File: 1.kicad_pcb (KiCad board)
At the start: 2 copper layers, 77.5 x 40.6 mm, 32 parts, among them IC1 LTC4361IDC-2#TRMPBF, IC2 SI1470DH-T1-E3, IC3 SI1470DH-T1-E3, IC4 LTC4361IDC-2#TRMPBF, J1 Screw_Terminal_01x03, J2 Screw_Terminal_01x01, J3 Screw_Terminal_01x01, J4 ON2, J5 ON1, U1 LTC2990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

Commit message: Patch
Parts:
- removed IC1, IC4: LTC4361IDC-2#TRMPBF, Library:SON45P200X200X80-9N-D
- removed IC2, IC3: SI1470DH-T1-E3, Library:SOT65P210X110-6N
- removed J4: ON2, Connector_PinHeader_1.00mm:PinHeader_1x01_P1.00mm_Vertical
- removed J5: ON1, Connector_PinHeader_1.00mm:PinHeader_1x01_P1.00mm_Vertical
- removed R3, R4: 0.025, 0.025 ohm rst:CRA2512-FZ-R025ELF
- R5, R6, R7: value 60m -> 50m; footprint 60 mil rst:RESC7146X175N -> 50m RST:RESC3216X88N
- moved U2 20.7 mm to (172.5, 78.7)
- moved SCLSDA1 20.6 mm to (175.0, 69.7)
- moved R6 20.6 mm to (171.7, 84.3)
- moved SCLSDA2 20.4 mm to (179.1, 89.0)
- moved R7 20.4 mm to (172.7, 100.3)
- moved U3 20.2 mm to (172.9, 94.0)
- moved U1 5.14 mm to (140.6, 73.7)
- moved R5 3.04 mm to (140.0, 79.1)
- moved C1 2.54 mm to (139.7, 96.5), turned to -90 degrees
- moved SCLSDA3 2.21 mm to (147.3, 70.8)
- moved J2 1.27 mm to (134.6, 71.1)
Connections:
- R6 pad 1: Net-(IC1-Pad3) -> Net-(Buck_IC1-Pad4)
- R7 pad 1: Net-(IC3-Pad4) -> Net-(Boost_IC1-Pad5)
- U2 pad 1: Net-(IC1-Pad3) -> Net-(Buck_IC1-Pad4)
- U2 pad 10: Net-(IC1-Pad3) -> Net-(Buck_IC1-Pad4)
- U3 pad 1: Net-(IC3-Pad4) -> Net-(Boost_IC1-Pad5)
- U3 pad 10: Net-(IC3-Pad4) -> Net-(Boost_IC1-Pad5)
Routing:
- net Earth: track 140.9 -> 90.6 mm, vias 7 -> 5
- net Net-(IC3-Pad4): track 38.0 -> 0.00 mm
- net Net-(IC1-Pad3): track 35.2 -> 0.00 mm
- net Net-(J1-Pad2): track 22.7 -> 0.00 mm
- net Net-(Buck_IC1-Pad4): track 60.0 -> 38.8 mm
- net Net-(Boost_IC1-Pad5): track 61.7 -> 43.2 mm
- net Net-(IC3-Pad1): track 16.5 -> 0.00 mm
- net Net-(Boost_IC1-Pad1): track 67.0 -> 52.2 mm
- net Net-(IC1-Pad7): track 14.1 -> 0.00 mm
- net Net-(J1-Pad1): track 16.3 -> 3.87 mm
- net Net-(SCLSDA2-Pad1): track 6.76 -> 19.0 mm
- net Net-(SCLSDA2-Pad2): track 7.41 -> 0.00 mm
- net Net-(J2-Pad1): track 27.3 -> 20.1 mm
- net Net-(IC3-Pad3): track 6.06 -> 0.00 mm
- net Net-(SCLSDA3-Pad1): track 5.83 -> 0.00 mm
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- removed copper zone on B.Cu, net Earth

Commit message: v1
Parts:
- Boost_IC1: footprint Boost LTC3426:SOT95P280X90-6N -> libs:SOT95P280X90-6N
- Buck_IC1: footprint BUck TPS62203DBVT:SOT95P280X145-5N -> libs:SOT95P280X145-5N
- C1, C4: footprint capa 10uf:CAPAE530X610N -> libs:CAPAE530X610N
- C2: footprint cap 22uF low esr and esl:C3216_Commercial -> libs:C3216_Commercial
- C3: footprint cap 4.7uf:C1210 -> libs:C1210
- D1: footprint Schottky dd:DIOM5026X220N -> libs:DIOM5026X220N
- J1: footprint TerminalBlock_MetzConnect:TerminalBlock_MetzConnect_Type055_RT01503HDWU_1x03_P5.00mm_Horizontal -> libs:TerminalBlock_MetzConnect_Type055_RT01503HDWU_1x03_P5.00mm_Horizontal
- J2, J3: footprint Connector_Pin:Pin_D1.3mm_L11.0mm_LooseFit -> libs:Pin_D1.3mm_L11.0mm_LooseFit
- L1: footprint indc 2.2uH:IHLP2020CZER2R2M8A -> libs:IHLP2020CZER2R2M8A
- L2: footprint indc 10uH crct:SRN1060-100M -> libs:SRN1060-100M
- R1: footprint rst 95.3k:RESC2012X60N -> libs:RESC2012X60N
- R2: footprint rst 30.9k:RC0603FR-0730K9L -> libs:RC0603FR-0730K9L
- R5, R6, R7: footprint 50m RST:RESC3216X88N -> libs:RESC3216X88N
- SCLSDA1, SCLSDA2, SCLSDA3, SHDN1: footprint Connector_PinHeader_1.00mm:PinHeader_1x02_P1.00mm_Vertical -> libs:PinHeader_1x02_P1.00mm_Vertical
- U1, U2, U3: footprint MON & PROTECC:SOP50P490X110-10N -> libs:SOP50P490X110-10N
- moved J1 21.7 mm to (182.9, 81.4)
- moved SCLSDA2 4.83 mm to (174.3, 88.6), turned to -90 degrees
- moved SHDN1 4.76 mm to (137.2, 89.5)
- moved SCLSDA1 2.88 mm to (174.0, 72.4), turned to -90 degrees
- moved R7 0.47 mm to (172.2, 100.3)
- moved R5 0.07 mm to (139.9, 79.1)
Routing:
- net Net-(J1-Pad2): track 0.00 -> 24.8 mm
- net Earth: track 90.6 -> 112.1 mm
- net Net-(Buck_IC1-Pad4): track 38.8 -> 60.0 mm
- net Net-(Boost_IC1-Pad5): track 43.2 -> 62.3 mm
- net Net-(SCLSDA2-Pad1): track 19.0 -> 3.31 mm
- net Net-(J1-Pad1): track 3.87 -> 14.9 mm
- net Net-(Boost_IC1-Pad1): track 52.2 -> 43.4 mm
- net Net-(SCLSDA3-Pad1): track 0.00 -> 5.98 mm
- net Net-(Boost_IC1-Pad4): track 25.7 -> 21.9 mm
- net Net-(J2-Pad1): track 20.1 -> 16.4 mm
- net Net-(SCLSDA1-Pad2): track 7.82 -> 4.14 mm
- net Net-(SCLSDA2-Pad2): track 0.00 -> 3.26 mm
- net Net-(Buck_IC1-Pad3): track 15.8 -> 13.3 mm
- net Net-(SCLSDA1-Pad1): track 6.32 -> 4.35 mm
- net Net-(SCLSDA3-Pad2): track 5.54 -> 7.49 mm
- added copper zone on B.Cu, net Earth
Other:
- board size 77.5 x 40.6 mm -> 55.9 x 35.6 mm

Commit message: Fixes + Patches
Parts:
- moved C1 0.32 mm to (140.0, 96.4)
- renumbered SCLSDA1 to I2C1, SCLSDA2 to I2C2, SCLSDA3 to I2C3, SHDN1 to SDN
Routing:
- net Earth: track 112.1 -> 70.7 mm
- net Net-(Boost_IC1-Pad1): track 43.4 -> 47.1 mm
- net Net-(J2-Pad1): track 16.4 -> 20.0 mm
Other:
- board text added: "CubeSat EPS Regulation Module"
- board text added: "GEC Barton Hill"

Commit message: Fix
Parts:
- removed SDN: EN, libs:PinHeader_1x02_P1.00mm_Vertical
- added R3: 1M, 1MEGA RST:RESC1608X55N, F.Cu at (147.0, 86.7)
- Boost_IC1: footprint libs:SOT95P280X90-6N -> Boost LTC3426:SOT95P280X90-6N
- Buck_IC1: footprint libs:SOT95P280X145-5N -> BUck TPS62203DBVT:SOT95P280X145-5N
- C1, C4: footprint libs:CAPAE530X610N -> capa 10uf:CAPAE530X610N
- C2: footprint libs:C3216_Commercial -> cap 22uF low esr and esl:C3216_Commercial
- C3: footprint libs:C1210 -> cap 4.7uf:C1210
- D1: footprint libs:DIOM5026X220N -> Schottky dd:DIOM5026X220N
- I2C1, I2C2, I2C3: footprint libs:PinHeader_1x02_P1.00mm_Vertical -> Connector_PinHeader_1.00mm:PinHeader_1x02_P1.00mm_Vertical
- J1: footprint libs:TerminalBlock_MetzConnect_Type055_RT01503HDWU_1x03_P5.00mm_Horizontal -> TerminalBlock_MetzConnect:TerminalBlock_MetzConnect_Type055_RT01503HDWU_1x03_P5.00mm_Horizontal
- J2, J3: footprint libs:Pin_D1.3mm_L11.0mm_LooseFit -> Connector_Pin:Pin_D1.3mm_L11.0mm_LooseFit
- L1: footprint libs:IHLP2020CZER2R2M8A -> indc 2.2uH:IHLP2020CZER2R2M8A
- L2: footprint libs:SRN1060-100M -> indc 10uH crct:SRN1060-100M
- R1: footprint libs:RESC2012X60N -> rst 95.3k:RESC2012X60N
- R2: footprint libs:RC0603FR-0730K9L -> rst 30.9k:RC0603FR-0730K9L
- R5, R6, R7: footprint libs:RESC3216X88N -> 50m RST:RESC3216X88N
- U1, U2, U3: footprint libs:SOP50P490X110-10N -> MON & PROTECC:SOP50P490X110-10N
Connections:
- Buck_IC1 pad 3: Net-(Buck_IC1-Pad3) -> Net-(Boost_IC1-Pad1)
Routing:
- net Net-(Buck_IC1-Pad3): track 13.3 -> 0.00 mm
- net Net-(Boost_IC1-Pad4): track 21.9 -> 14.9 mm
- net Net-(Boost_IC1-Pad1): track 47.1 -> 53.8 mm
- net Net-(Boost_IC1-Pad6): track 12.9 -> 15.8 mm
- net Earth: track 70.7 -> 68.3 mm, vias 5 -> 6

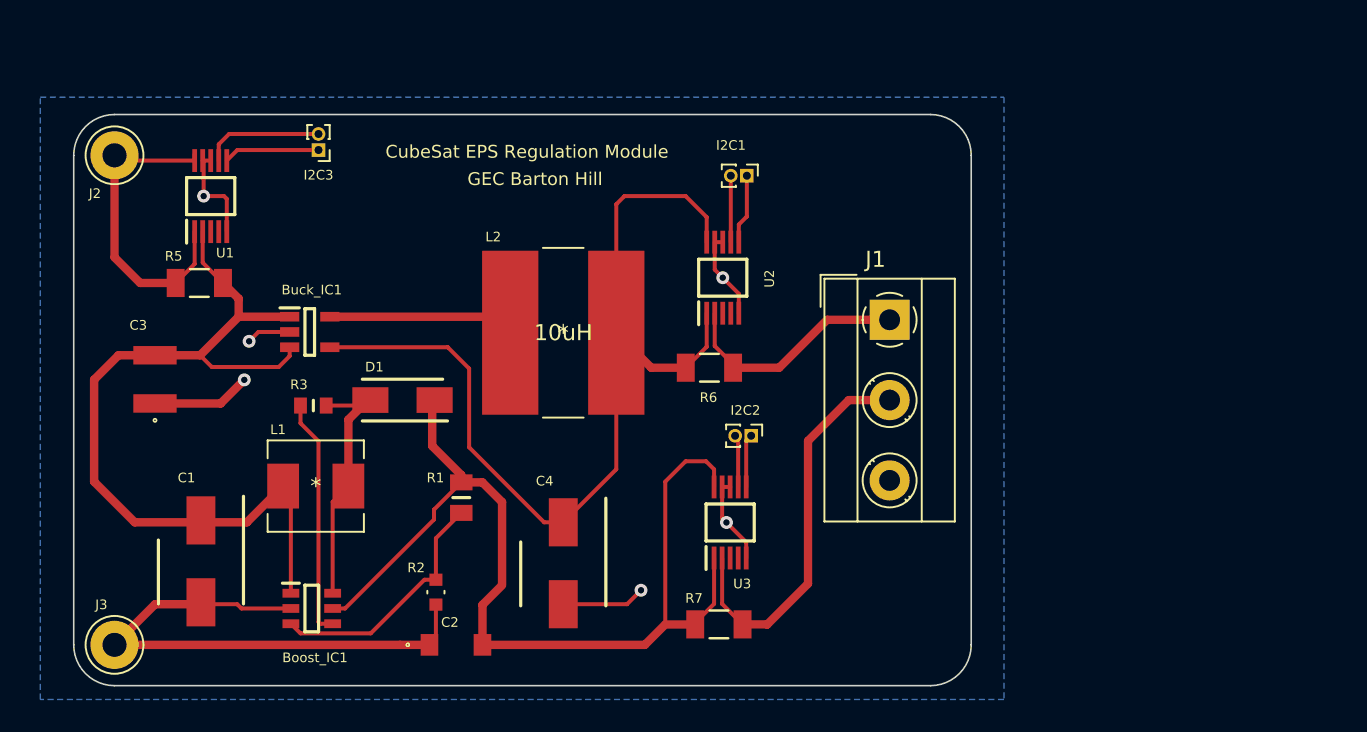
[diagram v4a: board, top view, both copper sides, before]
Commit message: Replaced Al elec caps
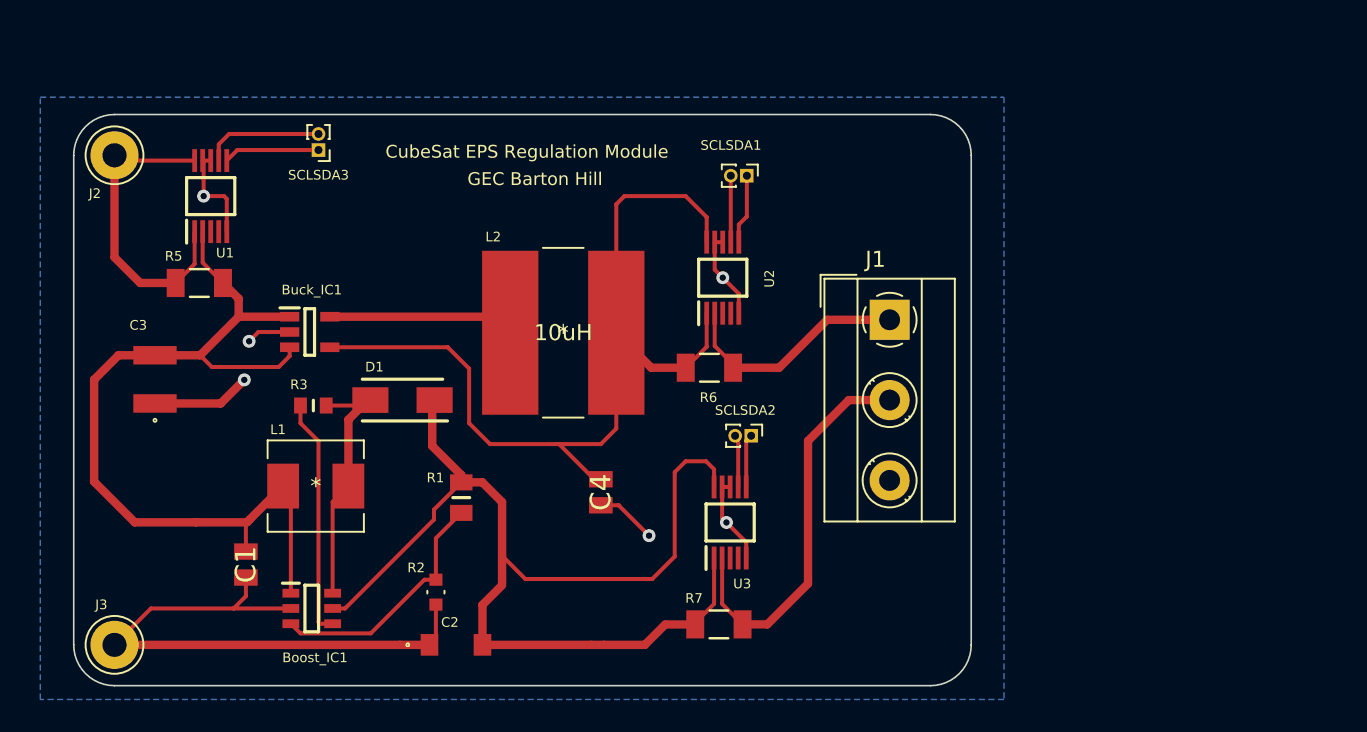
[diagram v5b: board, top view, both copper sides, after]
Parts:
- C1, C4: footprint capa 10uf:CAPAE530X610N -> 10uF MLCC:CAPC2012X94N
- moved C4 5.00 mm to (164.9, 92.1)
- moved C1 2.81 mm to (142.8, 96.6)
- renumbered I2C1 to SCLSDA1, I2C2 to SCLSDA2, I2C3 to SCLSDA3
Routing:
- net Net-(Boost_IC1-Pad5): track 62.3 -> 70.0 mm
- net Net-(Buck_IC1-Pad4): track 60.2 -> 57.3 mm
- net Net-(Boost_IC1-Pad1): track 53.8 -> 55.7 mm
- net Earth: track 68.3 -> 68.9 mm

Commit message: Fixed routing issues and naming of pins
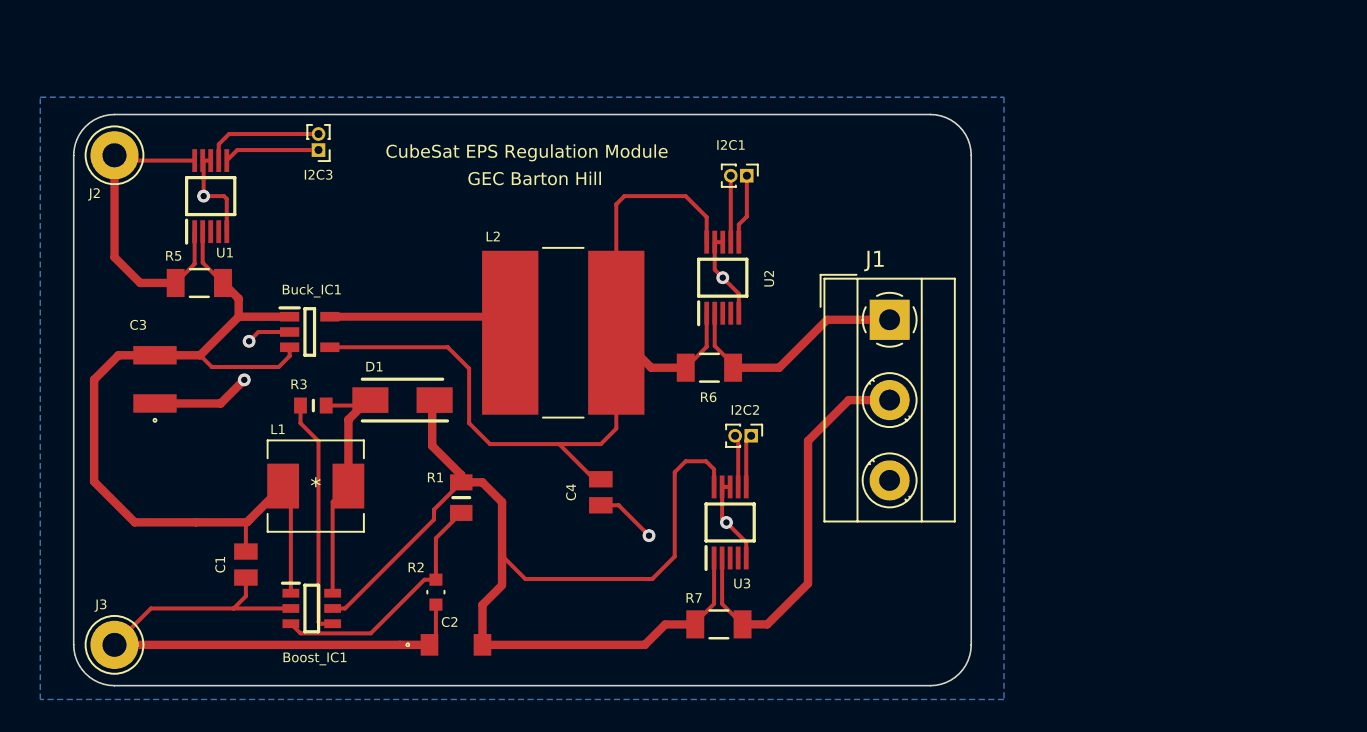
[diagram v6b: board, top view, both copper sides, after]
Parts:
- renumbered SCLSDA1 to I2C1, SCLSDA2 to I2C2, SCLSDA3 to I2C3
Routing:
- net Earth: track 68.9 -> 66.5 mm

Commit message: FInal...I guess
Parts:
- D1: footprint Schottky dd:DIOM5026X220N -> Schottky DD with stock:DIOM5126X265N
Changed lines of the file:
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@@
       (sketchpadsonfab false)
       (subtractmaskfromsilk false)
-      (outputformat 4)
+      (outputformat 1)
       (mirror false)
       (drillshape 0)
       (scaleselection 1)
-      (outputdirectory "/home/arch1/Desktop/")
+      (outputdirectory "/mnt/DAA829C1A8299CCF/EEE/S7/PROJ/voltage-regulator-module/Gerbers/")
     )
   )
@@
     )
   )
-  (footprint "Schottky dd:DIOM5026X220N" (layer "F.Cu")
+  (footprint "Schottky DD with stock:DIOM5126X265N" (layer "F.Cu")
     (at 152.55 86.36 180)
-    (descr "PMDS_SOD106")
-    (tags "Schottky Diode")
-    (property "Sheetfile" "1.kicad_sch")
-    (property "Sheetname" "")
-    (attr smd)
-    (fp_text reference "D1" (at 1.75 2.06 180) (layer "F.SilkS")
-      (effects (font (size 0.6 0.6) (thickness 0.15)))
+    (descr "SMA")
+    (tags "Diode")
+    (property "Sheetfile" "1.kicad_sch")
+    (property "Sheetname" "")
+    (attr smd)
+    (fp_text reference "D1" (at 0 0 180) (layer "F.SilkS")
+      (effects (font (size 1.27 1.27) (thickness 0.254)))
     )
     (fp_text value "D_Schottky" (at 0 0 180) (layer "F.SilkS") hide
@@
       (effects (font (size 1.27 1.27) (thickness 0.254)))
     )
-    (fp_line (start 2.5 -1.3) (end -2.8 -1.3) (layer "F.SilkS") (width 0.2))
-    (fp_line (start -2.5 1.3) (end 2.5 1.3) (layer "F.SilkS") (width 0.2))
-    (fp_line (start -3.375 1.65) (end -3.375 -1.65) (layer "F.CrtYd") (width 0.05))
-    (fp_line (start -3.375 -1.65) (end 3.375 -1.65) (layer "F.CrtYd") (width 0.05))
-    (fp_line (start 3.375 -1.65) (end 3.375 1.65) (layer "F.CrtYd") (width 0.05))
-    (fp_line (start 3.375 1.65) (end -3.375 1.65) (layer "F.CrtYd") (width 0.05))
-    (fp_line (start 2.5 1.3) (end -2.5 1.3) (layer "F.Fab") (width 0.1))
-    (fp_line (start -2.5 -0.5) (end -1.7 -1.3) (layer "F.Fab") (width 0.1))
-    (fp_line (start -2.5 1.3) (end -2.5 -1.3) (layer "F.Fab") (width 0.1))
-    (fp_line (start 2.5 -1.3) (end 2.5 1.3) (layer "F.Fab") (width 0.1))
-    (fp_line (start -2.5 -1.3) (end 2.5 -1.3) (layer "F.Fab") (width 0.1))
-    (pad "1" smd rect (at -2 0 270) (size 1.6 2.25) (layers "F.Cu" "F.Paste" "F.Mask")
+    (fp_line (start -2.538 1.288) (end 2.538 1.288) (layer "F.SilkS") (width 0.2))
+    (fp_line (start 2.538 -1.288) (end -2.825 -1.288) (layer "F.SilkS") (width 0.2))
+    (fp_line (start -3.4 1.7) (end -3.4 -1.7) (layer "F.CrtYd") (width 0.05))
+    (fp_line (start 3.4 1.7) (end -3.4 1.7) (layer "F.CrtYd") (width 0.05))
+    (fp_line (start -3.4 -1.7) (end 3.4 -1.7) (layer "F.CrtYd") (width 0.05))
+    (fp_line (start 3.4 -1.7) (end 3.4 1.7) (layer "F.CrtYd") (width 0.05))
+    (fp_line (start 2.538 1.288) (end -2.538 1.288) (layer "F.Fab") (width 0.1))
+    (fp_line (start -2.538 -0.512) (end -1.762 -1.288) (layer "F.Fab") (width 0.1))
+    (fp_line (start -2.538 1.288) (end -2.538 -1.288) (layer "F.Fab") (width 0.1))
+    (fp_line (start 2.538 -1.288) (end 2.538 1.288) (layer "F.Fab") (width 0.1))
+    (fp_line (start -2.538 -1.288) (end 2.538 -1.288) (layer "F.Fab") (width 0.1))
+    (pad "1" smd rect (at -2.05 0 270) (size 1.55 2.2) (layers "F.Cu" "F.Paste" "F.Mask")
       (net 8 "Net-(Boost_IC1-Pad5)") (pinfunction "K") (pintype "passive"))
-    (pad "2" smd rect (at 2 0 270) (size 1.6 2.25) (layers "F.Cu" "F.Paste" "F.Mask")
+    (pad "2" smd rect (at 2.05 0 270) (size 1.55 2.2) (layers "F.Cu" "F.Paste" "F.Mask")
       (net 5 "Net-(Boost_IC1-Pad6)") (pinfunction "A") (pintype "passive"))
-    (model "RBR3L40ADDTE25.stp"
-      (offset (xyz 0 0 0))
-      (scale (xyz 1 1 1))
-      (rotate (xyz 0 0 0))
-    )
-    (model "/mnt/DAA829C1A8299CCF/EEE/S7/PROJ/COMPS/Schottky/LIB_RBR3L40ADDTE25/RBR3L40ADDTE25/3D/RBR3L40ADDTE25.stp"
-      (offset (xyz 0 0 0))
-      (scale (xyz 1 1 1))
-      (rotate (xyz 0 0 0))
+    (model "STPS2150A.stp" hide
+      (offset (xyz 0 0 0.23))
+      (scale (xyz 1 1 1))
+      (rotate (xyz 0 0 -180))
+    )
+    (model "/mnt/DAA829C1A8299CCF/EEE/S7/PROJ/COMPS/Schottky/LIB_STPS2150A stock ond/STPS2150A/3D/STPS2150A.stp"
+      (offset (xyz 0 0 1.1))
+      (scale (xyz 1 1 1))
+      (rotate (xyz 0 0 0))

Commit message: sch edits
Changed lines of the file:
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@@
     (property "Sheetname" "")
     (attr smd)
-    (fp_text reference "D1" (at 0 0 180) (layer "F.SilkS")
+    (fp_text reference "D1" (at -0.1435 -3.64 180) (layer "F.SilkS")
       (effects (font (size 1.27 1.27) (thickness 0.254)))
     )
